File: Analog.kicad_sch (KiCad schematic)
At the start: 11 parts, among them IC1 AMC1350DWVR

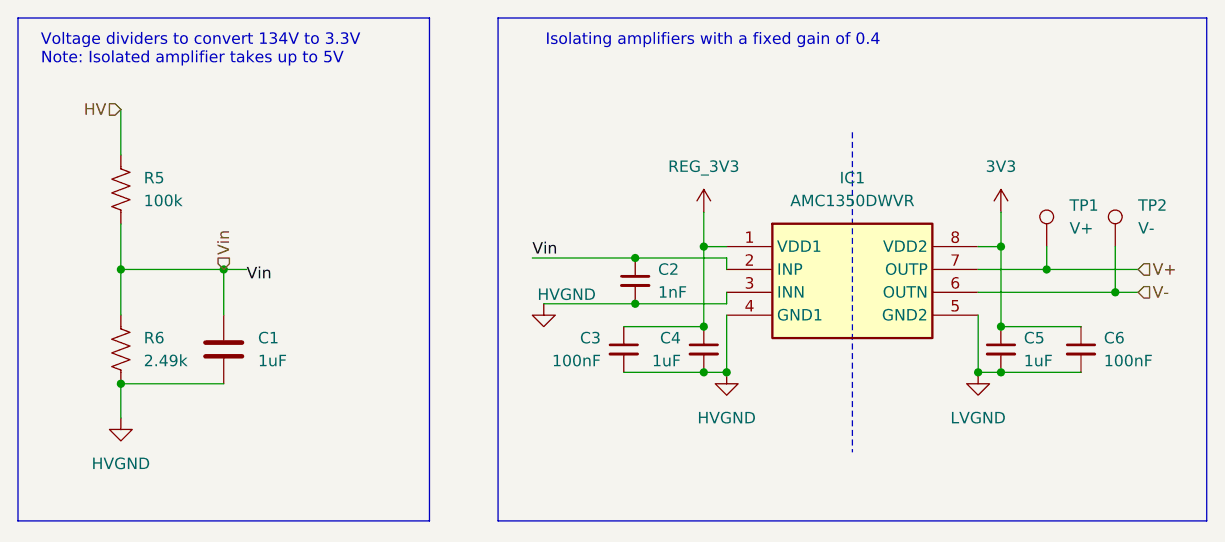
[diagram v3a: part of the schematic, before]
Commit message: Did some of the initial layout after schematic changes, concerned about the choking on how i currently have the opamp kind of set up, also havent touched the testpoints yet so that will probably make it more complex
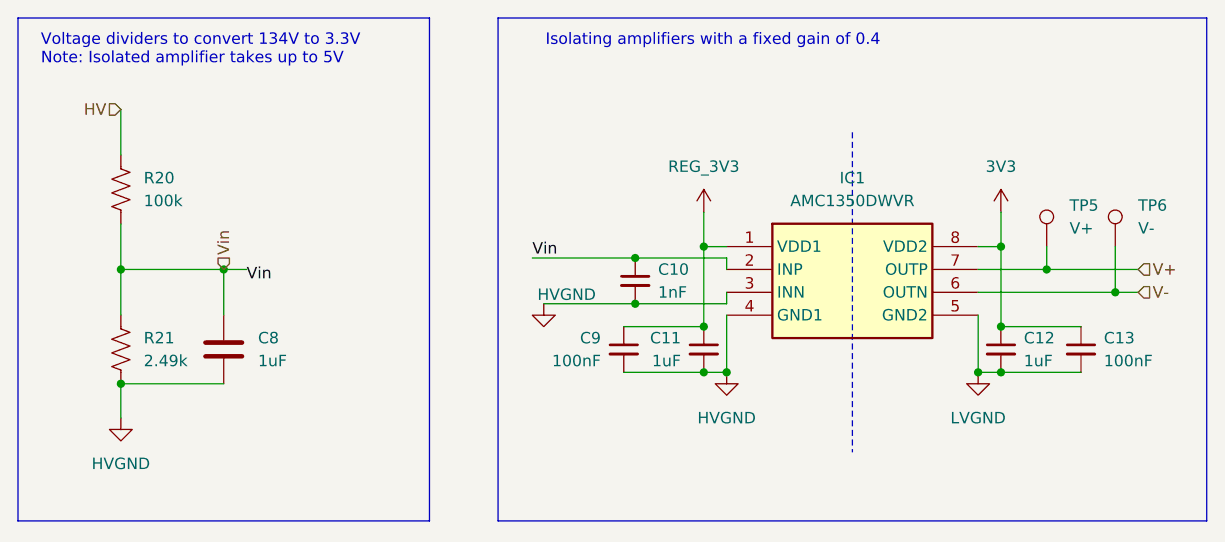
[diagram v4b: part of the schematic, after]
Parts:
- renumbered C2 to C10, C4 to C11, C5 to C12, C6 to C13, C1 to C8, C3 to C9, R5 to R20, R6 to R21, TP1 to TP5, TP2 to TP6
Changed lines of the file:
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@@
 		(on_board yes)
 		(dnp no)
-		(property "Reference" "C2"
+		(property "Reference" "C10"
 			(at 91.44 48.2662 0)
 			(effects
@@
 			(project "ActivePrecharge RevB"
 				(path "/5b79bd62-039b-48b8-a776-6011f31800bf/66508218-a57e-446c-8ad7-eed26f1cbb2f"
-					(reference "C8")
-					(unit 1)
-				)
-				(path "/5b79bd62-039b-48b8-a776-6011f31800bf/b87ed4ab-ede8-4401-aaa8-4c2bfd6c5f57"
-					(reference "C2")
+					(reference "C16")
+					(unit 1)
+				)
+				(path "/5b79bd62-039b-48b8-a776-6011f31800bf/b87ed4ab-ede8-4401-aaa8-4c2bfd6c5f57"
+					(reference "C10")
 					(unit 1)
 				)
@@
 		(on_board yes)
 		(dnp no)
-		(property "Reference" "#PWR028"
+		(property "Reference" "#PWR037"
 			(at 78.74 58.42 0)
 			(effects
@@
 			(project "ActivePrecharge RevB"
 				(path "/5b79bd62-039b-48b8-a776-6011f31800bf/66508218-a57e-446c-8ad7-eed26f1cbb2f"
-					(reference "#PWR027")
-					(unit 1)
-				)
-				(path "/5b79bd62-039b-48b8-a776-6011f31800bf/b87ed4ab-ede8-4401-aaa8-4c2bfd6c5f57"
-					(reference "#PWR028")
+					(reference "#PWR043")
+					(unit 1)
+				)
+				(path "/5b79bd62-039b-48b8-a776-6011f31800bf/b87ed4ab-ede8-4401-aaa8-4c2bfd6c5f57"
+					(reference "#PWR037")
 					(unit 1)
 				)
@@
 		(on_board yes)
 		(dnp no)
-		(property "Reference" "C3"
+		(property "Reference" "C9"
 			(at 85.09 55.8862 0)
 			(effects
@@
 			(project "ActivePrecharge RevB"
 				(path "/5b79bd62-039b-48b8-a776-6011f31800bf/66508218-a57e-446c-8ad7-eed26f1cbb2f"
+					(reference "C15")
+					(unit 1)
+				)
+				(path "/5b79bd62-039b-48b8-a776-6011f31800bf/b87ed4ab-ede8-4401-aaa8-4c2bfd6c5f57"
 					(reference "C9")
-					(unit 1)
-				)
-				(path "/5b79bd62-039b-48b8-a776-6011f31800bf/b87ed4ab-ede8-4401-aaa8-4c2bfd6c5f57"
-					(reference "C3")
 					(unit 1)
 				)
@@
 		(dnp no)
 		(fields_autoplaced yes)
-		(property "Reference" "#PWR036"
+		(property "Reference" "#PWR041"
 			(at 129.54 45.72 0)
 			(effects
@@
 			(project "ActivePrecharge RevB"
 				(path "/5b79bd62-039b-48b8-a776-6011f31800bf/66508218-a57e-446c-8ad7-eed26f1cbb2f"
-					(reference "#PWR035")
-					(unit 1)
-				)
-				(path "/5b79bd62-039b-48b8-a776-6011f31800bf/b87ed4ab-ede8-4401-aaa8-4c2bfd6c5f57"
-					(reference "#PWR036")
+					(reference "#PWR047")
+					(unit 1)
+				)
+				(path "/5b79bd62-039b-48b8-a776-6011f31800bf/b87ed4ab-ede8-4401-aaa8-4c2bfd6c5f57"
+					(reference "#PWR041")
 					(unit 1)
 				)
@@
 		(on_board yes)
 		(dnp no)
-		(property "Reference" "C6"
+		(property "Reference" "C13"
 			(at 140.97 55.8862 0)
 			(effects
@@
 			(project "ActivePrecharge RevB"
 				(path "/5b79bd62-039b-48b8-a776-6011f31800bf/66508218-a57e-446c-8ad7-eed26f1cbb2f"
-					(reference "C12")
-					(unit 1)
-				)
-				(path "/5b79bd62-039b-48b8-a776-6011f31800bf/b87ed4ab-ede8-4401-aaa8-4c2bfd6c5f57"
-					(reference "C6")
+					(reference "C19")
+					(unit 1)
+				)
+				(path "/5b79bd62-039b-48b8-a776-6011f31800bf/b87ed4ab-ede8-4401-aaa8-4c2bfd6c5f57"
+					(reference "C13")
 					(unit 1)
 				)
@@
 		(dnp no)
 		(fields_autoplaced yes)
-		(property "Reference" "TP2"
+		(property "Reference" "TP6"
 			(at 144.78 41.1479 0)
 			(effects
@@
 			(project "ActivePrecharge RevB"
 				(path "/5b79bd62-039b-48b8-a776-6011f31800bf/66508218-a57e-446c-8ad7-eed26f1cbb2f"
-					(reference "TP4")
-					(unit 1)
-				)
-				(path "/5b79bd62-039b-48b8-a776-6011f31800bf/b87ed4ab-ede8-4401-aaa8-4c2bfd6c5f57"
-					(reference "TP2")
+					(reference "TP8")
+					(unit 1)
+				)
+				(path "/5b79bd62-039b-48b8-a776-6011f31800bf/b87ed4ab-ede8-4401-aaa8-4c2bfd6c5f57"
+					(reference "TP6")
 					(unit 1)
 				)
@@
 		(dnp no)
 		(fields_autoplaced yes)
-		(property "Reference" "TP1"
+		(property "Reference" "TP5"
 			(at 137.16 41.1479 0)
 			(effects
@@
 			(project "ActivePrecharge RevB"
 				(path "/5b79bd62-039b-48b8-a776-6011f31800bf/66508218-a57e-446c-8ad7-eed26f1cbb2f"
-					(reference "TP3")
-					(unit 1)
-				)
-				(path "/5b79bd62-039b-48b8-a776-6011f31800bf/b87ed4ab-ede8-4401-aaa8-4c2bfd6c5f57"
-					(reference "TP1")
+					(reference "TP7")
+					(unit 1)
+				)
+				(path "/5b79bd62-039b-48b8-a776-6011f31800bf/b87ed4ab-ede8-4401-aaa8-4c2bfd6c5f57"
+					(reference "TP5")
 					(unit 1)
 				)
@@
 		(on_board yes)
 		(dnp no)
-		(property "Reference" "C4"
+		(property "Reference" "C11"
 			(at 93.98 55.8862 0)
 			(effects
@@
 			(project "ActivePrecharge RevB"
 				(path "/5b79bd62-039b-48b8-a776-6011f31800bf/66508218-a57e-446c-8ad7-eed26f1cbb2f"
-					(reference "C10")
-					(unit 1)
-				)
-				(path "/5b79bd62-039b-48b8-a776-6011f31800bf/b87ed4ab-ede8-4401-aaa8-4c2bfd6c5f57"
-					(reference "C4")
+					(reference "C17")
+					(unit 1)
+				)
+				(path "/5b79bd62-039b-48b8-a776-6011f31800bf/b87ed4ab-ede8-4401-aaa8-4c2bfd6c5f57"
+					(reference "C11")
 					(unit 1)
 				)
@@
 		(dnp no)
 		(fields_autoplaced yes)
-		(property "Reference" "#PWR034"
+		(property "Reference" "#PWR040"
 			(at 127 66.04 0)
 			(effects
@@
 			(project "ActivePrecharge RevB"
 				(path "/5b79bd62-039b-48b8-a776-6011f31800bf/66508218-a57e-446c-8ad7-eed26f1cbb2f"
-					(reference "#PWR033")
-					(unit 1)
-				)
-				(path "/5b79bd62-039b-48b8-a776-6011f31800bf/b87ed4ab-ede8-4401-aaa8-4c2bfd6c5f57"
-					(reference "#PWR034")
+					(reference "#PWR046")
+					(unit 1)
+				)
+				(path "/5b79bd62-039b-48b8-a776-6011f31800bf/b87ed4ab-ede8-4401-aaa8-4c2bfd6c5f57"
+					(reference "#PWR040")
 					(unit 1)
 				)
@@
 		(dnp no)
 		(fields_autoplaced yes)
-		(property "Reference" "R5"
+		(property "Reference" "R20"
 			(at 34.29 38.0999 0)
 			(effects
@@
 			(project "ActivePrecharge RevB"
 				(path "/5b79bd62-039b-48b8-a776-6011f31800bf/66508218-a57e-446c-8ad7-eed26f1cbb2f"
-					(reference "R7")
-					(unit 1)
-				)
-				(path "/5b79bd62-039b-48b8-a776-6011f31800bf/b87ed4ab-ede8-4401-aaa8-4c2bfd6c5f57"
-					(reference "R5")
+					(reference "R22")
+					(unit 1)
+				)
+				(path "/5b79bd62-039b-48b8-a776-6011f31800bf/b87ed4ab-ede8-4401-aaa8-4c2bfd6c5f57"
+					(reference "R20")
 					(unit 1)
 				)
@@
 		(dnp no)
 		(fields_autoplaced yes)
-		(property "Reference" "#PWR026"
+		(property "Reference" "#PWR036"
 			(at 31.75 71.12 0)
 			(effects
@@
 			(project "ActivePrecharge RevB"
 				(path "/5b79bd62-039b-48b8-a776-6011f31800bf/66508218-a57e-446c-8ad7-eed26f1cbb2f"
-					(reference "#PWR09")
-					(unit 1)
-				)
-				(path "/5b79bd62-039b-48b8-a776-6011f31800bf/b87ed4ab-ede8-4401-aaa8-4c2bfd6c5f57"
-					(reference "#PWR026")
+					(reference "#PWR042")
+					(unit 1)
+				)
+				(path "/5b79bd62-039b-48b8-a776-6011f31800bf/b87ed4ab-ede8-4401-aaa8-4c2bfd6c5f57"
+					(reference "#PWR036")
 					(unit 1)
 				)
@@
 		(dnp no)
 		(fields_autoplaced yes)
-		(property "Reference" "C1"
+		(property "Reference" "C8"
 			(at 46.99 55.8799 0)
 			(effects
@@
 			(project "ActivePrecharge RevB"
 				(path "/5b79bd62-039b-48b8-a776-6011f31800bf/66508218-a57e-446c-8ad7-eed26f1cbb2f"
-					(reference "C7")
-					(unit 1)
-				)
-				(path "/5b79bd62-039b-48b8-a776-6011f31800bf/b87ed4ab-ede8-4401-aaa8-4c2bfd6c5f57"
-					(reference "C1")
+					(reference "C14")
+					(unit 1)
+				)
+				(path "/5b79bd62-039b-48b8-a776-6011f31800bf/b87ed4ab-ede8-4401-aaa8-4c2bfd6c5f57"
+					(reference "C8")
 					(unit 1)
 				)
@@
 		(dnp no)
 		(fields_autoplaced yes)
-		(property "Reference" "R6"
+		(property "Reference" "R21"
 			(at 34.29 55.8799 0)
 			(effects
@@
 			(project "ActivePrecharge RevB"
 				(path "/5b79bd62-039b-48b8-a776-6011f31800bf/66508218-a57e-446c-8ad7-eed26f1cbb2f"
-					(reference "R8")
-					(unit 1)
-				)
-				(path "/5b79bd62-039b-48b8-a776-6011f31800bf/b87ed4ab-ede8-4401-aaa8-4c2bfd6c5f57"
-					(reference "R6")
+					(reference "R23")
+					(unit 1)
+				)
+				(path "/5b79bd62-039b-48b8-a776-6011f31800bf/b87ed4ab-ede8-4401-aaa8-4c2bfd6c5f57"
+					(reference "R21")
 					(unit 1)
 				)
@@
 		(dnp no)
 		(fields_autoplaced yes)
-		(property "Reference" "#PWR032"
+		(property "Reference" "#PWR039"
 			(at 99.06 66.04 0)
 			(effects
@@
 			(project "ActivePrecharge RevB"
 				(path "/5b79bd62-039b-48b8-a776-6011f31800bf/66508218-a57e-446c-8ad7-eed26f1cbb2f"
-					(reference "#PWR031")
-					(unit 1)
-				)
-				(path "/5b79bd62-039b-48b8-a776-6011f31800bf/b87ed4ab-ede8-4401-aaa8-4c2bfd6c5f57"
-					(reference "#PWR032")
+					(reference "#PWR045")
+					(unit 1)
+				)
+				(path "/5b79bd62-039b-48b8-a776-6011f31800bf/b87ed4ab-ede8-4401-aaa8-4c2bfd6c5f57"
+					(reference "#PWR039")
 					(unit 1)
 				)
@@
 		(on_board yes)
 		(dnp no)
-		(property "Reference" "C5"
+		(property "Reference" "C12"
 			(at 132.08 55.8862 0)
 			(effects
@@
 			(project "ActivePrecharge RevB"
 				(path "/5b79bd62-039b-48b8-a776-6011f31800bf/66508218-a57e-446c-8ad7-eed26f1cbb2f"
-					(reference "C11")
-					(unit 1)
-				)
-				(path "/5b79bd62-039b-48b8-a776-6011f31800bf/b87ed4ab-ede8-4401-aaa8-4c2bfd6c5f57"
-					(reference "C5")
+					(reference "C18")
+					(unit 1)
+				)
+				(path "/5b79bd62-039b-48b8-a776-6011f31800bf/b87ed4ab-ede8-4401-aaa8-4c2bfd6c5f57"
+					(reference "C12")
 					(unit 1)
 				)
@@
 		(on_board yes)
 		(dnp no)
-		(property "Reference" "#PWR030"
+		(property "Reference" "#PWR038"
 			(at 96.52 45.72 0)
 			(effects
@@
 			(project "ActivePrecharge RevB"
 				(path "/5b79bd62-039b-48b8-a776-6011f31800bf/66508218-a57e-446c-8ad7-eed26f1cbb2f"
-					(reference "#PWR029")
-					(unit 1)
-				)
-				(path "/5b79bd62-039b-48b8-a776-6011f31800bf/b87ed4ab-ede8-4401-aaa8-4c2bfd6c5f57"
-					(reference "#PWR030")
-					(unit 1)
-				)
+					(reference "#PWR044")
+					(unit 1)
+				)
+				(path "/5b79bd62-039b-48b8-a776-6011f31800bf/b87ed4ab-ede8-4401-aaa8-4c2bfd6c5f57"
+					(reference "#PWR038")
+					(unit 1)
+				)

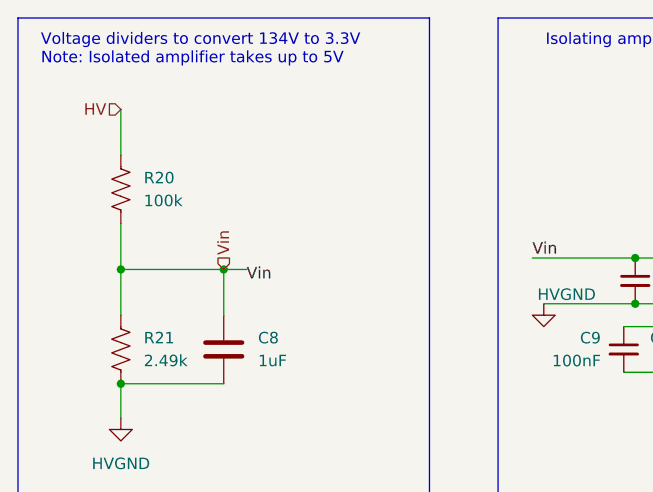
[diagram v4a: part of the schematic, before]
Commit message: Made all layout changes. Ready for review. Also deleted some unnecessary files to clean up the libraries.
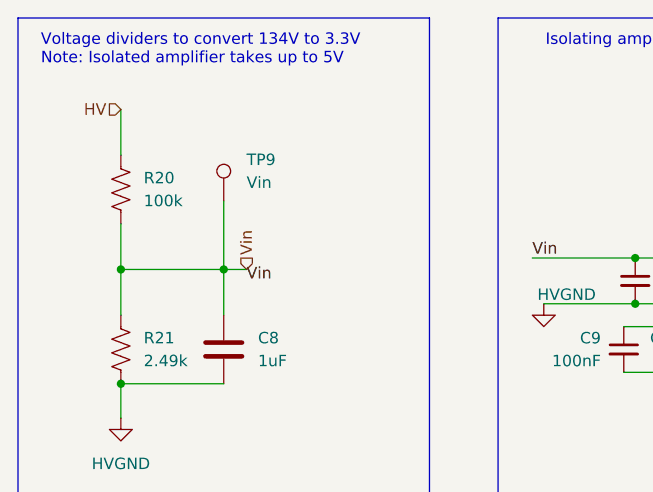
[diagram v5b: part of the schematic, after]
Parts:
- added TP9: Vin, TestPoint:TestPoint_Keystone_5005-5009_Compact, symbol Connector:TestPoint
- TP5, TP6: footprint TestPoint:TestPoint_Pad_2.0x2.0mm -> TestPoint:TestPoint_Keystone_5005-5009_Compact
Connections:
- net Vin: now also TP9.1
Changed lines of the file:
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@@
+	(wire
+		(pts
+			(xy 43.18 40.64) (xy 43.18 48.26)
+		)
+		(stroke
+			(width 0)
+			(type default)
+		)
+	)
 	(wire
 		(pts
@@
 	(hierarchical_label "Vin"
 		(shape input)
-		(at 43.18 48.26 90)
+		(at 45.72 48.26 90)
 		(effects
 			(font
@@
 			)
 		)
-		(property "Footprint" "TestPoint:TestPoint_Pad_2.0x2.0mm"
+		(property "Footprint" "TestPoint:TestPoint_Keystone_5005-5009_Compact"
 			(at 147.32 45.72 0)
 			(effects
@@
 			)
 		)
-		(property "Footprint" "TestPoint:TestPoint_Pad_2.0x2.0mm"
+		(property "Footprint" "TestPoint:TestPoint_Keystone_5005-5009_Compact"
 			(at 139.7 45.72 0)
 			(effects
@@
 					(unit 1)
 				)
+			)
+		)
+	)
+	(symbol
+		(lib_id "Connector:TestPoint")
+		(at 43.18 40.64 0)
+		(unit 1)
+		(exclude_from_sim no)
+		(in_bom yes)
+		(on_board yes)
+		(dnp no)
+		(fields_autoplaced yes)
+		(property "Reference" "TP9"
+			(at 45.72 36.0679 0)
+			(effects
+				(font
+					(size 1.27 1.27)
+				)
+				(justify left)
+			)
+		)
+		(property "Value" "Vin"
+			(at 45.72 38.6079 0)
+			(effects
+				(font
+					(size 1.27 1.27)
+				)
+				(justify left)
+			)
+		)
+		(property "Footprint" "TestPoint:TestPoint_Keystone_5005-5009_Compact"
+			(at 48.26 40.64 0)
+			(effects
+				(font
+					(size 1.27 1.27)
+				)
+				(hide yes)
+			)
+		)
+		(property "Datasheet" "~"
+			(at 48.26 40.64 0)
+			(effects
+				(font
+					(size 1.27 1.27)
+				)
+				(hide yes)
+			)
+		)
+		(property "Description" "test point"
+			(at 43.18 40.64 0)
+			(effects
+				(font
+					(size 1.27 1.27)
+				)
+				(hide yes)
+			)
+		)
+		(pin "1"
+		)
+		(instances
+			(project ""
+				(path "/5b79bd62-039b-48b8-a776-6011f31800bf/66508218-a57e-446c-8ad7-eed26f1cbb2f"
+					(reference "TP10")
+					(unit 1)
+				)
+				(path "/5b79bd62-039b-48b8-a776-6011f31800bf/b87ed4ab-ede8-4401-aaa8-4c2bfd6c5f57"
+					(reference "TP9")
+					(unit 1)
+				)
